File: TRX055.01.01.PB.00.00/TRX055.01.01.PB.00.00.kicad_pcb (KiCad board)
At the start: 4 copper layers, 91.3 x 139.8 mm, 164 parts, among them J1 DF40HC-80DS, J2 DF40HC-80DS, J3 DF40HC-80DS, J4 DF40HC-80DS, J5 SFP, J6 Micro_SD_Card, U1 XC7Z015-1CLG485I, U11 KSZ9031RNXCA, U12 USB3320C-EZK-TR, U14 W25Q128JVSIQ, U2 K4B4G1646E-BYMA, U3 K4B4G1646E-BYMA, U5 AP22913CN4, U9 AP22913CN4

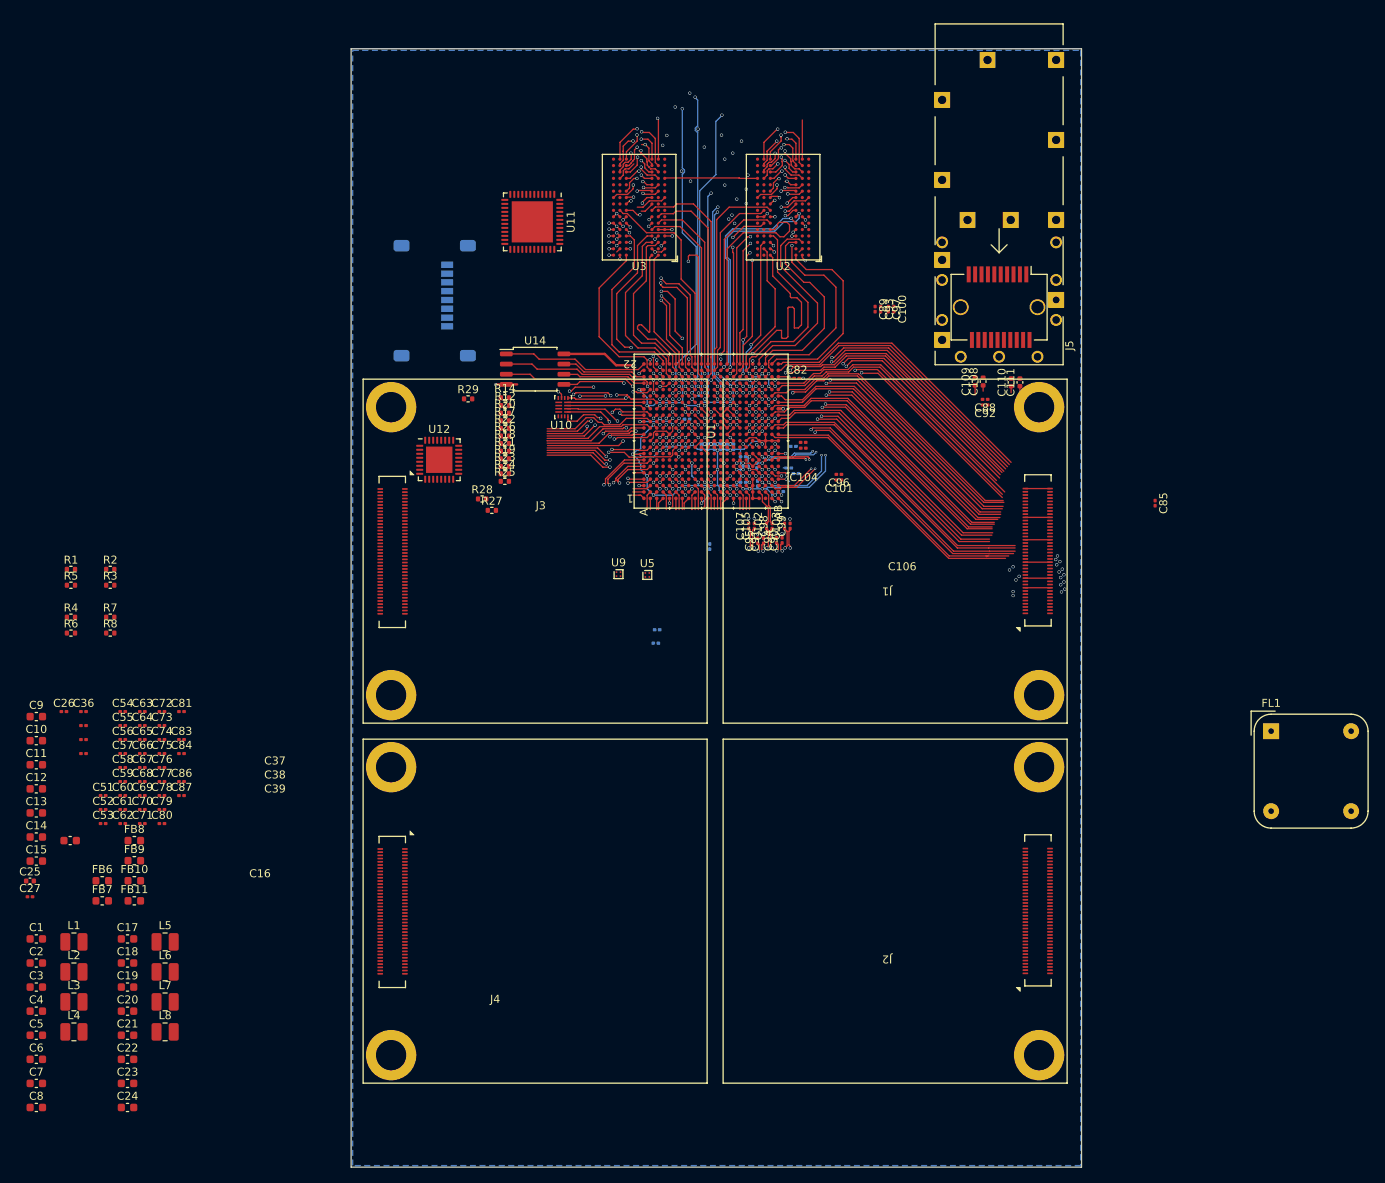
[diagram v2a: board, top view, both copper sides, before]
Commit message: +ETH +USB +Connectors
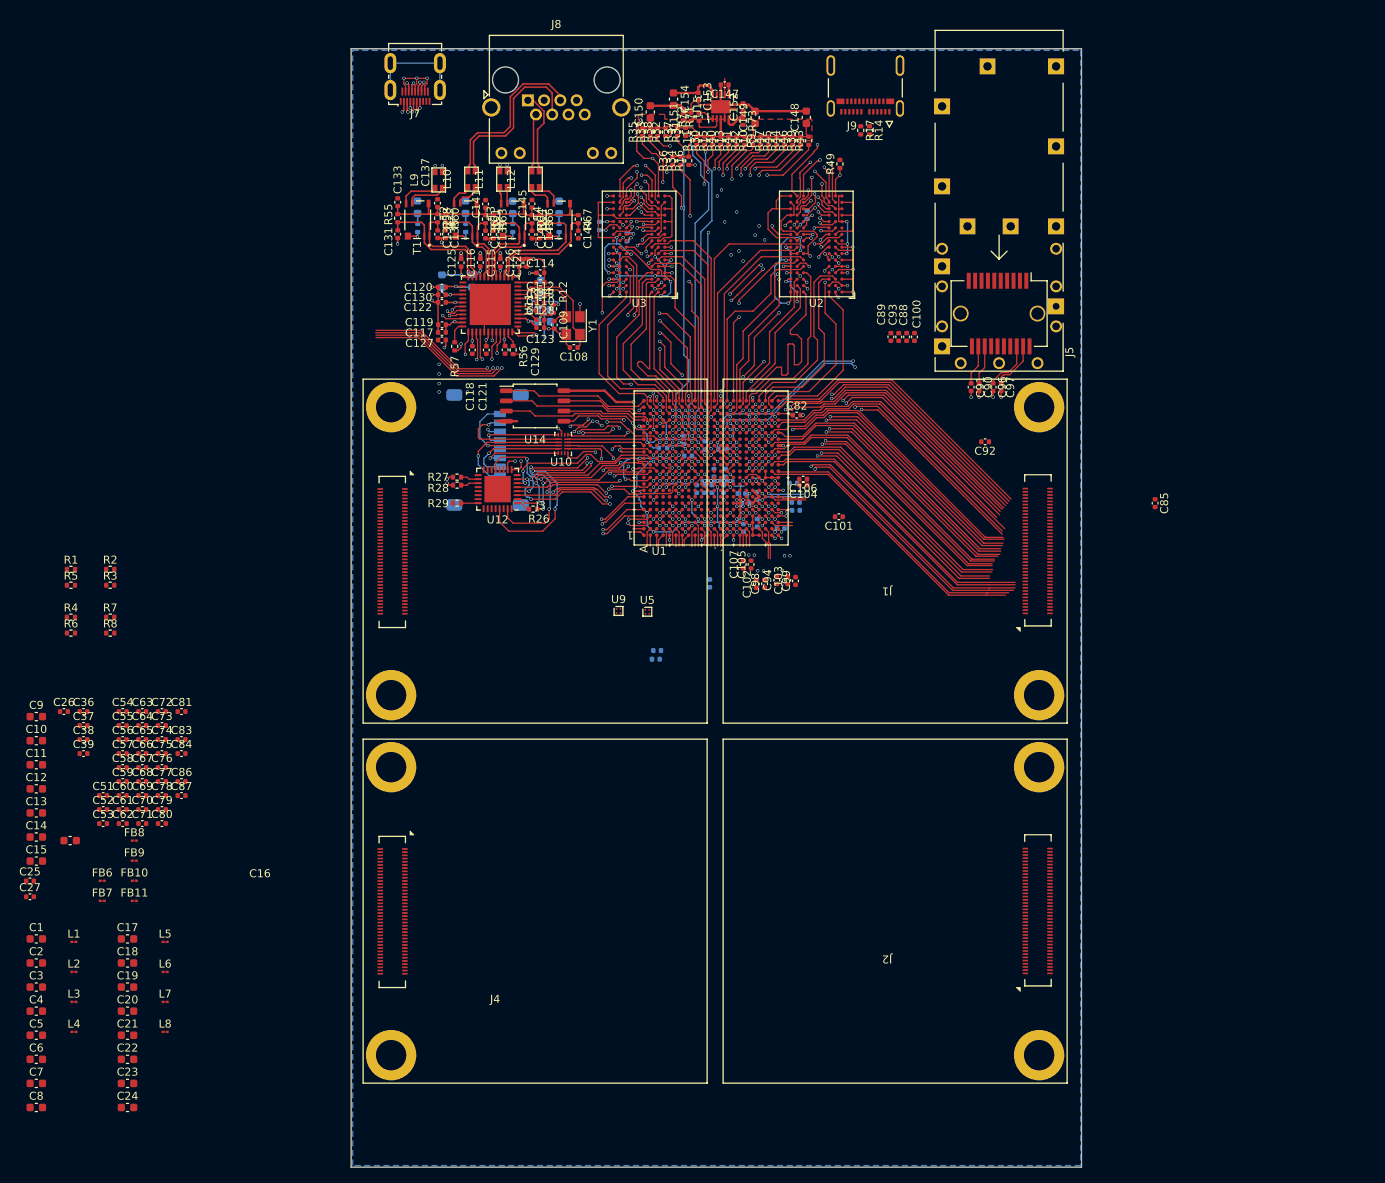
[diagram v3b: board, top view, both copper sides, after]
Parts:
- removed C111: M1, Capacitor_SMD:C_0402_1005Metric
- removed C95: M1, Capacitor_SMD:C_0201_0603Metric
- removed FL1: Choke_Schaffner_RN102-0.3-02-12M, Inductor_THT:Choke_Schaffner_RN102-04-14.0x14.0mm
- removed R18, R19, R20, R21, R22, R23, R24, R25: 33R, Resistor_SMD:R_0402_1005Metric
- added C112: M1, Capacitor_SMD:C_0402_1005Metric, F.Cu at (83.7, 61.0)
- added C113: 1M, Capacitor_SMD:C_0402_1005Metric, F.Cu at (83.7, 62.0)
- added C114: 1M, Capacitor_SMD:C_0402_1005Metric, F.Cu at (83.7, 58.2)
- added C115: M1, Capacitor_SMD:C_0402_1005Metric, F.Cu at (78.7, 57.0)
- added C116: M1, Capacitor_SMD:C_0402_1005Metric, F.Cu at (76.2, 56.9)
- added C117: 1M, Capacitor_SMD:C_0402_1005Metric, F.Cu at (71.3, 65.7)
- added C118: M1, Capacitor_SMD:C_0402_1005Metric, F.Cu at (75.2, 67.8)
- added C119: M1, Capacitor_SMD:C_0402_1005Metric, F.Cu at (71.4, 64.7)
- added C120: M1, Capacitor_SMD:C_0402_1005Metric, F.Cu at (71.3, 60.0)
- added C121: M1, Capacitor_SMD:C_0402_1005Metric, F.Cu at (76.9, 67.8)
- added C122: M1, Capacitor_SMD:C_0402_1005Metric, F.Cu at (71.3, 61.9)
- added C123: M1, Capacitor_SMD:C_0402_1005Metric, F.Cu at (83.7, 65.0)
- added C124: 1M, Capacitor_SMD:C_0402_1005Metric, F.Cu at (82.0, 57.0)
- added C125: M1, Capacitor_SMD:C_0402_1005Metric, F.Cu at (73.8, 57.0)
- added C126: M1, Capacitor_SMD:C_0402_1005Metric, F.Cu at (81.0, 57.0)
- added C127: 1M, Capacitor_SMD:C_0402_1005Metric, F.Cu at (71.3, 66.6)
- added C128: M1, Capacitor_SMD:C_0402_1005Metric, F.Cu at (83.7, 64.1)
- added C129: M1, Capacitor_SMD:C_0402_1005Metric, F.Cu at (79.2, 67.8)
- added C130: M1, Capacitor_SMD:C_0402_1005Metric, F.Cu at (71.3, 61.0)
- added C131: 10P, Capacitor_SMD:C_0402_1005Metric, F.Cu at (65.8, 53.4)
- added C132: 10P, Capacitor_SMD:C_0402_1005Metric, F.Cu at (70.8, 53.4)
- added C133: M1, Capacitor_SMD:C_0402_1005Metric, F.Cu at (65.8, 49.4)
- added C134: 1N, Capacitor_SMD:C_0603_1608Metric, B.Cu at (68.3, 50.0)
- added C135: 10P, Capacitor_SMD:C_0402_1005Metric, F.Cu at (71.8, 53.4)
- added C136: 10P, Capacitor_SMD:C_0402_1005Metric, F.Cu at (76.8, 53.4)
- added C137: M1, Capacitor_SMD:C_0402_1005Metric, F.Cu at (70.8, 49.5)
- added C138: 1N, Capacitor_SMD:C_0603_1608Metric, B.Cu at (74.3, 50.0)
- added C139: 10P, Capacitor_SMD:C_0402_1005Metric, F.Cu at (77.8, 53.4)
- added C140: 10P, Capacitor_SMD:C_0402_1005Metric, F.Cu at (82.6, 53.4)
- added C141: M1, Capacitor_SMD:C_0402_1005Metric, F.Cu at (76.8, 49.6)
- added C142: 1N, Capacitor_SMD:C_0603_1608Metric, B.Cu at (80.2, 50.0)
- added C143: 10P, Capacitor_SMD:C_0402_1005Metric, F.Cu at (83.6, 53.4)
- added C144: 10P, Capacitor_SMD:C_0402_1005Metric, F.Cu at (88.4, 53.4)
- added C145: M1, Capacitor_SMD:C_0402_1005Metric, F.Cu at (82.6, 49.6)
- added C146: 1N, Capacitor_SMD:C_0603_1608Metric, B.Cu at (86.0, 50.0)
- added C147: M1, Capacitor_SMD:C_0402_1005Metric, F.Cu at (106.7, 34.7)
- added C148: 10M, Capacitor_SMD:C_0603_1608Metric, F.Cu at (116.9, 38.8)
- added C149: 10M, Capacitor_SMD:C_0603_1608Metric, F.Cu at (110.5, 38.8)
- added C150: 10M, Capacitor_SMD:C_0603_1608Metric, F.Cu at (97.4, 38.1)
- added C151: M1, Capacitor_SMD:C_0402_1005Metric, F.Cu at (101.5, 38.7)
- added C152: M1, Capacitor_SMD:C_0402_1005Metric, F.Cu at (109.0, 37.5)
- added C153: M1, Capacitor_SMD:C_0402_1005Metric, F.Cu at (103.4, 36.2)
- added C154: 10M, Capacitor_SMD:C_0603_1608Metric, F.Cu at (100.3, 36.5)
- added FB1: GZ1608D601TF, Inductor_SMD:L_0603_1608Metric, B.Cu at (75.1, 59.2)
- added FB2: GZ1608D601TF, Inductor_SMD:L_0603_1608Metric, B.Cu at (84.1, 64.3)
- added FB3: GZ1608D601TF, Inductor_SMD:L_0603_1608Metric, B.Cu at (71.3, 59.2)
- added FB4: GZ1608D601TF, Inductor_SMD:L_0603_1608Metric, B.Cu at (84.1, 62.8)
- added FB5: GZ1608D601TF, Inductor_SMD:L_0603_1608Metric, B.Cu at (83.7, 59.9)
- added J7: HDMI_D_1.4, foot-ppa-passive:HDMI_Micro-D_Molex_46765-1x01, F.Cu at (68.0, 32.0)
- added J8: RJHSE5383, Connector_RJ:RJ45_Amphenol_RJHSE538X, F.Cu at (82.1, 36.6)
- added J9: 1054500101, 1054500101:MOLEX_1054500101, F.Cu at (124.3, 30.5)
- added L10: SRF2012A-801Y, foot-ppa-passive:SRF2012A-801Y, F.Cu at (75.0, 46.5)
- added L11: SRF2012A-801Y, foot-ppa-passive:SRF2012A-801Y, F.Cu at (79.0, 46.5)
- added L12: SRF2012A-801Y, foot-ppa-passive:SRF2012A-801Y, F.Cu at (83.0, 46.5)
- added L9: SRF2012A-801Y, foot-ppa-passive:SRF2012A-801Y, F.Cu at (70.9, 46.6)
- added R10: 39R, Resistor_SMD:R_0402_1005Metric, F.Cu at (110.2, 41.7)
- added R11: 39R, Resistor_SMD:R_0402_1005Metric, F.Cu at (103.2, 41.7)
- added R13: 39R, Resistor_SMD:R_0402_1005Metric, F.Cu at (107.2, 41.7)
- added R15: 39R, Resistor_SMD:R_0402_1005Metric, F.Cu at (105.2, 41.7)
- added R16: 39R, Resistor_SMD:R_0402_1005Metric, F.Cu at (102.2, 44.2)
- added R30: 39R, Resistor_SMD:R_0402_1005Metric, F.Cu at (104.2, 41.7)
- added R31: 39R, Resistor_SMD:R_0402_1005Metric, F.Cu at (101.8, 40.6)
- added R32: 39R, Resistor_SMD:R_0402_1005Metric, F.Cu at (99.3, 40.6)
- added R33: 39R, Resistor_SMD:R_0402_1005Metric, F.Cu at (97.4, 40.6)
- added R34: 39R, Resistor_SMD:R_0402_1005Metric, F.Cu at (101.2, 44.2)
- added R35: 39R, Resistor_SMD:R_0402_1005Metric, F.Cu at (96.4, 40.6)
- added R36: 39R, Resistor_SMD:R_0402_1005Metric, F.Cu at (100.2, 44.2)
- added R37: 39R, Resistor_SMD:R_0402_1005Metric, F.Cu at (100.8, 40.6)
- added R38: 39R, Resistor_SMD:R_0402_1005Metric, F.Cu at (98.3, 40.6)
- added R39: 39R, Resistor_SMD:R_0402_1005Metric, F.Cu at (116.2, 41.7)
- added R40: 39R, Resistor_SMD:R_0402_1005Metric, F.Cu at (106.2, 41.7)
- added R41: 39R, Resistor_SMD:R_0402_1005Metric, F.Cu at (108.2, 41.7)
- added R42: 39R, Resistor_SMD:R_0402_1005Metric, F.Cu at (109.2, 41.7)
- added R43: 39R, Resistor_SMD:R_0402_1005Metric, F.Cu at (117.2, 41.7)
- added R44: 39R, Resistor_SMD:R_0402_1005Metric, F.Cu at (114.2, 41.7)
- added R45: 39R, Resistor_SMD:R_0402_1005Metric, F.Cu at (113.2, 41.7)
- added R46: 39R, Resistor_SMD:R_0402_1005Metric, F.Cu at (115.2, 41.7)
- added R47: 39R, Resistor_SMD:R_0402_1005Metric, F.Cu at (112.2, 41.7)
- added R48: 80R, Resistor_SMD:R_0402_1005Metric, B.Cu at (94.5, 53.8)
- added R49: 10K, Resistor_SMD:R_0402_1005Metric, F.Cu at (121.1, 44.6)
- added R50: 240R, Resistor_SMD:R_0402_1005Metric, B.Cu at (117.0, 51.0)
- added R51: 240R, Resistor_SMD:R_0402_1005Metric, B.Cu at (91.0, 52.4)
- added R52: 80R, Resistor_SMD:R_0402_1005Metric, B.Cu at (106.4, 80.2)
- added R53: 80R, Resistor_SMD:R_0402_1005Metric, B.Cu at (104.2, 79.8)
- added R54: ???, Resistor_SMD:R_0402_1005Metric, F.Cu at (83.7, 59.5)
- added R55: 49R9, Resistor_SMD:R_0402_1005Metric, F.Cu at (65.8, 51.4)
- added R56: 33R, Resistor_SMD:R_0402_1005Metric, F.Cu at (80.2, 67.8)
- added R57: 33R, Resistor_SMD:R_0402_1005Metric, F.Cu at (73.0, 67.4)
- added R58: 49R9, Resistor_SMD:R_0402_1005Metric, F.Cu at (70.8, 51.4)
- added R59: 75R, Resistor_SMD:R_0402_1005Metric, B.Cu at (68.3, 52.6)
- added R60: 49R9, Resistor_SMD:R_0402_1005Metric, F.Cu at (71.8, 51.4)
- added R61: 49R9, Resistor_SMD:R_0402_1005Metric, F.Cu at (76.8, 51.5)
- added R62: 75R, Resistor_SMD:R_0402_1005Metric, B.Cu at (74.3, 52.6)
- added R63: 49R9, Resistor_SMD:R_0402_1005Metric, F.Cu at (77.8, 51.5)
- added R64: 49R9, Resistor_SMD:R_0402_1005Metric, F.Cu at (82.6, 51.5)
- added R65: 75R, Resistor_SMD:R_0402_1005Metric, B.Cu at (80.2, 52.6)
- added R66: 49R9, Resistor_SMD:R_0402_1005Metric, F.Cu at (83.6, 51.5)
- added R67: 49R9, Resistor_SMD:R_0402_1005Metric, F.Cu at (88.4, 51.5)
- added R68: 75R, Resistor_SMD:R_0402_1005Metric, B.Cu at (86.0, 52.6)
- added R69: 10K, Resistor_SMD:R_0402_1005Metric, B.Cu at (101.6, 79.1)
- added R70: 10K, Resistor_SMD:R_0402_1005Metric, B.Cu at (99.0, 80.1)
- added R71: 10K, Resistor_SMD:R_0402_1005Metric, F.Cu at (103.5, 38.7)
- added R72: 10K, Resistor_SMD:R_0402_1005Metric, F.Cu at (102.5, 38.7)
- added R73: 33R, Resistor_SMD:R_0402_1005Metric, F.Cu at (109.0, 39.2)
- added R9: 39R, Resistor_SMD:R_0402_1005Metric, F.Cu at (111.2, 41.7)
- added T1: SM453229-231N7Y, snapeda:XFMR_SM453229-231N7Y, F.Cu at (68.3, 51.6)
- added T2: SM453229-231N7Y, snapeda:XFMR_SM453229-231N7Y, F.Cu at (74.3, 51.6)
- added T3: SM453229-231N7Y, snapeda:XFMR_SM453229-231N7Y, F.Cu at (80.2, 51.6)
- added T4: SM453229-231N7Y, snapeda:XFMR_SM453229-231N7Y, F.Cu at (86.0, 51.6)
- added U15: TPS51200DRC, Package_SON:VSON-10-1EP_3x3mm_P0.5mm_EP1.65x2.4mm, F.Cu at (106.2, 37.5)
- added Y1: X322525MOB4SI, Crystal:Crystal_SMD_3225-4Pin_3.2x2.5mm, F.Cu at (87.8, 64.8)
- C100, C101, C102, C103, C104, C105, C106, C107, C26, C27, C28, C29, C30, C31, C32, C33, C34, C35, C36, C37, C38, C39, C40, C41, C42, C43, C44, C45, C46, C47, C48, C49, C50, C51, C52, C53, C54, C55, C56, C57, C58, C59, C60, C61, C62, C63, C64, C65, C66, C67, C68, C69, C70, C71, C72, C73, C74, C75, C76, C77, C78, C79, C80, C81, C82, C83, C84, C85, C86, C87, C88, C89, C90, C91, C92, C93, C94, C96, C97, C98, C99: footprint Capacitor_SMD:C_0201_0603Metric -> Capacitor_SMD:C_0402_1005Metric
- C108, C109: value M1 -> 10P
- FB10, FB11, FB6, FB7, FB8, FB9: footprint Inductor_SMD:L_0603_1608Metric -> Resistor_SMD:R_01005_0402Metric
- L1, L2, L3, L4, L5, L6, L7, L8: footprint Inductor_SMD:L_1008_2520Metric -> Resistor_SMD:R_01005_0402Metric
- R12: value 33R -> 10K
- moved C110 59.5 mm to (83.7, 63.0), turned to 0 degrees
- moved R17 57.4 mm to (123.7, 40.4), turned to -90 degrees
- moved R14 56.5 mm to (124.8, 40.4), turned to -90 degrees
- moved C109 53.1 mm to (85.4, 64.7), turned to -90 degrees
- moved C108 51.3 mm to (87.8, 67.5), turned to 180 degrees
- moved C91 32.3 mm to (137.5, 72.5), turned to -90 degrees
- moved C90 31.2 mm to (138.5, 72.5), turned to -90 degrees
- moved C96 22.1 mm to (140.2, 72.5), turned to -90 degrees
- moved J6 19.8 mm to (76.5, 80.3)
- moved C97 17.1 mm to (141.2, 72.5)
- moved R12 13.5 mm to (85.3, 62.7), turned to -90 degrees
- moved R29 13.1 mm to (73.2, 87.0)
- moved C88 12.5 mm to (129.4, 66.2), turned to -90 degrees
- moved U11 11.6 mm to (77.4, 62.2)
- moved R26 9.81 mm to (82.8, 87.8)
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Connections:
- C108 pad 1: Net-(J5-RD+) -> Net-(U11-XI)
- C108 pad 2: /SFP_Port/SFP_RX_P -> GND
- C109 pad 1: Net-(J5-RD-) -> Net-(U11-XO)
- C109 pad 2: /SFP_Port/SFP_RX_N -> GND
- C110 pad 1: Net-(J5-TD+) -> Net-(U11-RESET_N)
- C110 pad 2: /SFP_Port/SFP_TX_P -> GND
- C12 pad 1: /ZynqPower/1V8_RAIL_A -> +1V8
- C36 pad 1: VCC_MIO -> +1V8
- C37 pad 1: VCC_MIO -> +1V8
- C38 pad 1: VCC_MIO -> +1V8
- C39 pad 1: VCC_MIO -> +1V8
- C57 pad 1: /ZynqPower/1V8_RAIL_A -> +1V8
- C58 pad 1: /ZynqPower/1V8_RAIL_A -> +1V8
- C59 pad 1: /ZynqPower/1V8_RAIL_A -> +1V8
- C60 pad 1: /ZynqPower/1V8_RAIL_A -> +1V8
- C61 pad 1: /ZynqPower/VCCDDR -> VDD_DDR
- C62 pad 1: /ZynqPower/VCCDDR -> VDD_DDR
- C63 pad 1: /ZynqPower/VCCDDR -> VDD_DDR
- C64 pad 1: /ZynqPower/VCCDDR -> VDD_DDR
- C65 pad 1: /ZynqPower/VCCDDR -> VDD_DDR
- C66 pad 1: /ZynqPower/VCCDDR -> VDD_DDR
- C67 pad 1: /ZynqPower/VCCDDR -> VDD_DDR
- C68 pad 1: /ZynqPower/VCCDDR -> VDD_DDR
- C69 pad 1: /ZynqPower/VCCDDR -> VDD_DDR
- C7 pad 1: /ZynqPower/1V8_RAIL_A -> +1V8
- C8 pad 1: /ZynqPower/1V8_RAIL_A -> +1V8
- FB11 pad 1: VCC_MIO -> +1V8
- FB6 pad 1: /ZynqPower/1V8_RAIL_A -> +1V8
- FB7 pad 2: /ZynqPower/VCCDDR -> VDD_DDR
- J5 pad 12: Net-(J5-RD-) -> /GT_RX0_N
- J5 pad 13: Net-(J5-RD+) -> /GT_RX0_P
- J5 pad 15: Net-(J5-VccR) -> +3V3
- J5 pad 16: Net-(J5-VccR) -> +3V3
- J5 pad 18: Net-(J5-TD+) -> /GT_TX0_P
- J5 pad 19: Net-(J5-TD-) -> /GT_TX0_N
- J6 pad 1: unconnected-(J6-DAT2-Pad1) -> Net-(J6-DAT2)
- J6 pad 2: unconnected-(J6-DAT3/CD-Pad2) -> Net-(J6-DAT3/CD)
- J6 pad 3: unconnected-(J6-CMD-Pad3) -> Net-(J6-CMD)
- J6 pad 4: unconnected-(J6-VDD-Pad4) -> +3V3
- J6 pad 5: unconnected-(J6-CLK-Pad5) -> Net-(J6-CLK)
- J6 pad 6: unconnected-(J6-VSS-Pad6) -> GND
- J6 pad 7: unconnected-(J6-DAT0-Pad7) -> Net-(J6-DAT0)
- J6 pad 8: unconnected-(J6-DAT1-Pad8) -> Net-(J6-DAT1)
- J6 pad 9: unconnected-(J6-SHIELD-Pad9) -> GND
- L4 pad 2: /ZynqPower/1V8_RAIL_A -> +1V8
- R12 pad 1: Net-(U12-NXT) -> DVDDH
- R12 pad 2: /Zynq_PSMIO/MIO_ULPI_NXT -> Net-(U11-RESET_N)
- R14 pad 1: Net-(U12-STP) -> /USB_C/USBC_DP
- R14 pad 2: /Zynq_PSMIO/MIO_ULPI_STP -> /USB_C/USB_DP
- R17 pad 1: Net-(U12-DIR) -> /USB_C/USBC_DM
- R17 pad 2: /Zynq_PSMIO/MIO_ULPI_DIR -> /USB_C/USB_DM
- R27 pad 1: unconnected-(R27-Pad1) -> /USB_C/USB_DP
- R28 pad 1: unconnected-(R28-Pad1) -> /USB_C/USB_DM
- U1 pad A13: VCC_MIO -> +1V8
- U1 pad A4: unconnected-(U1B-IO_L10N_T1_AD11N_35-PadA4) -> /TMDS_D0_P
- U1 pad A5: unconnected-(U1B-IO_L10P_T1_AD11P_35-PadA5) -> /TMDS_D0_N
- U1 pad A6: unconnected-(U1B-IO_L9N_T1_DQS_AD3N_35-PadA6) -> /TMDS_CLK_P
- U1 pad A7: unconnected-(U1B-IO_L9P_T1_DQS_AD3P_35-PadA7) -> /TMDS_CLK_N
- U1 pad B10: VCC_MIO -> +1V8
- U1 pad B20: VCC_MIO -> +1V8
- U1 pad B3: unconnected-(U1B-IO_L13N_T2_MRCC_35-PadB3) -> /TMDS_D2_P
- U1 pad B4: unconnected-(U1B-IO_L13P_T2_MRCC_35-PadB4) -> /TMDS_D2_N
- U1 pad C11: unconnected-(U1D-PS_MIO53_501-PadC11) -> /ETH_PHY_Metal/SMI_MDIO
- U1 pad C17: VCC_MIO -> +1V8
- U1 pad D13: unconnected-(U1D-PS_MIO52_501-PadD13) -> /ETH_PHY_Metal/SMI_MDC
- U1 pad D14: VCC_MIO -> +1V8
- U1 pad E11: VCC_MIO -> +1V8
- U1 pad E21: /ZynqPower/VCCDDR -> VDD_DDR
- U1 pad E5: unconnected-(U1B-IO_L5N_T0_AD9N_35-PadE5) -> /TMDS_D1_P
- U1 pad F15: unconnected-(U1E-PS_MIO_VREF_501-PadF15) -> /ZynqPower/PS_MIO_VREF_501
- U1 pad F18: /ZynqPower/VCCDDR -> VDD_DDR
- U1 pad F5: unconnected-(U1B-IO_L5P_T0_AD9P_35-PadF5) -> /TMDS_D1_N
- U1 pad H16: unconnected-(U1E-PS_DDR_VREF0_502-PadH16) -> /ZynqPower/DDRVREF
- U1 pad H22: /ZynqPower/VCCDDR -> VDD_DDR
- U1 pad J19: /ZynqPower/VCCDDR -> VDD_DDR
- U1 pad K14: /ZynqPower/1V8_RAIL_A -> +1V8
- U1 pad K16: /ZynqPower/VCCDDR -> VDD_DDR
- U1 pad L13: /ZynqPower/1V8_RAIL_A -> +1V8
- U1 pad M14: /ZynqPower/1V8_RAIL_A -> +1V8
- U1 pad M16: unconnected-(U1C-PS_DDR_VRN_502-PadM16) -> Net-(U1C-PS_DDR_VRN_502)
- U1 pad M20: /ZynqPower/VCCDDR -> VDD_DDR
- U1 pad N13: VCC_MIO -> +1V8
- U1 pad N16: unconnected-(U1C-PS_DDR_VRP_502-PadN16) -> Net-(U1C-PS_DDR_VRP_502)
- U1 pad N17: /ZynqPower/VCCDDR -> VDD_DDR
- U1 pad P12: VCC_MIO -> +1V8
- U1 pad P14: /ZynqPower/1V8_RAIL_A -> +1V8
- U1 pad P16: unconnected-(U1E-PS_DDR_VREF1_502-PadP16) -> /ZynqPower/DDRVREF
- U1 pad R13: VCC_MIO -> +1V8
- U1 pad R21: /ZynqPower/VCCDDR -> VDD_DDR
- U1 pad T12: VCC_MIO -> +1V8
- U1 pad V22: /ZynqPower/VCCDDR -> VDD_DDR
- U10 pad 10: unconnected-(U10-DAT0B-Pad10) -> Net-(J6-DAT2)
- U10 pad 11: unconnected-(U10-DAT3B-Pad11) -> Net-(J6-DAT1)
- U10 pad 12: unconnected-(U10-DAT2B-Pad12) -> Net-(J6-DAT3/CD)
- U10 pad 13: unconnected-(U10-CMDB-Pad13) -> Net-(J6-CMD)
- U10 pad 15: VCC_MIO -> +1V8
- U10 pad 8: unconnected-(U10-CLKB-Pad8) -> Net-(J6-CLK)
- U10 pad 9: unconnected-(U10-DAT1B-Pad9) -> Net-(J6-DAT0)
- U11 pad 1: unconnected-(U11-AVDDH-Pad1) -> AVDDH
- U11 pad 10: unconnected-(U11-TXRXP_D-Pad10) -> /ETH_PHY_Metal/ETH_Pair/MDI_IN_P
- U11 pad 11: unconnected-(U11-TXRXM_D-Pad11) -> /ETH_PHY_Metal/ETH_Pair/MDI_IN_N
- U11 pad 12: unconnected-(U11-AVDDH-Pad12) -> AVDDH
- U11 pad 14: unconnected-(U11-DVDDL-Pad14) -> DVDDL
- U11 pad 16: unconnected-(U11-DVDDH-Pad16) -> DVDDH
- U11 pad 18: unconnected-(U11-DVDDL-Pad18) -> DVDDL
- U11 pad 19: unconnected-(U11-TXD0-Pad19) -> /Zynq_PSMIO/MIO_RGMII_TX0
- U11 pad 2: unconnected-(U11-TXRXP_A-Pad2) -> /ETH_PHY_Metal/ETH_Pair3/MDI_IN_P
- U11 pad 20: unconnected-(U11-TXD1-Pad20) -> /Zynq_PSMIO/MIO_RGMII_TX1
- U11 pad 21: unconnected-(U11-TXD2-Pad21) -> /Zynq_PSMIO/MIO_RGMII_TX2
- U11 pad 22: unconnected-(U11-TXD3-Pad22) -> /Zynq_PSMIO/MIO_RGMII_TX3
- U11 pad 23: unconnected-(U11-DVDDL-Pad23) -> DVDDL
- U11 pad 24: unconnected-(U11-GTX_CLK-Pad24) -> Net-(U11-GTX_CLK)
- U11 pad 25: unconnected-(U11-TX_EN-Pad25) -> /Zynq_PSMIO/MIO_RGMII_TX_CTL
- U11 pad 26: unconnected-(U11-DVDDL-Pad26) -> DVDDL
- U11 pad 27: unconnected-(U11-RXD3/MODE3-Pad27) -> /Zynq_PSMIO/MIO_RGMII_RX3
- U11 pad 28: unconnected-(U11-RXD2/MODE2-Pad28) -> /Zynq_PSMIO/MIO_RGMII_RX2
- U11 pad 29: unconnected-(U11-VSS-Pad29) -> GND
- U11 pad 3: unconnected-(U11-TXRXM_A-Pad3) -> /ETH_PHY_Metal/ETH_Pair3/MDI_IN_N
- U11 pad 30: unconnected-(U11-DVDDL-Pad30) -> DVDDL
- U11 pad 31: unconnected-(U11-RXD1/MODE1-Pad31) -> /Zynq_PSMIO/MIO_RGMII_RX1
- U11 pad 32: unconnected-(U11-RXD0/MODE0-Pad32) -> /Zynq_PSMIO/MIO_RGMII_RX0
- U11 pad 33: unconnected-(U11-RX_DV/CLK125_EN-Pad33) -> /Zynq_PSMIO/MIO_RGMII_RX_CTL
- U11 pad 34: unconnected-(U11-DVDDH-Pad34) -> DVDDH
- U11 pad 35: unconnected-(U11-RX_CLK/PHYAD2-Pad35) -> Net-(U11-RX_CLK/PHYAD2)
- U11 pad 36: unconnected-(U11-MDC-Pad36) -> /ETH_PHY_Metal/SMI_MDC
- U11 pad 37: unconnected-(U11-MDIO-Pad37) -> /ETH_PHY_Metal/SMI_MDIO
- U11 pad 39: unconnected-(U11-DVDDL-Pad39) -> DVDDL
- U11 pad 4: unconnected-(U11-AVDDL-Pad4) -> AVDDL
- U11 pad 40: unconnected-(U11-DVDDH-Pad40) -> DVDDH
- U11 pad 42: unconnected-(U11-RESET_N-Pad42) -> Net-(U11-RESET_N)
- U11 pad 44: unconnected-(U11-AVDDL_PLL-Pad44) -> AVDDL_PLL
- U11 pad 45: unconnected-(U11-XO-Pad45) -> Net-(U11-XO)
- U11 pad 46: unconnected-(U11-XI-Pad46) -> Net-(U11-XI)
- U11 pad 48: unconnected-(U11-ISET-Pad48) -> Net-(U11-ISET)
- U11 pad 49: unconnected-(U11-PAD_GND-Pad49) -> GND
- U11 pad 5: unconnected-(U11-TXRXP_B-Pad5) -> /ETH_PHY_Metal/ETH_Pair2/MDI_IN_P
- U11 pad 6: unconnected-(U11-TXRXM_B-Pad6) -> /ETH_PHY_Metal/ETH_Pair2/MDI_IN_N
- U11 pad 7: unconnected-(U11-TXRXP_C-Pad7) -> /ETH_PHY_Metal/ETH_Pair1/MDI_IN_P
- U11 pad 8: unconnected-(U11-TXRXM_C-Pad8) -> /ETH_PHY_Metal/ETH_Pair1/MDI_IN_N
- U11 pad 9: unconnected-(U11-AVDDL-Pad9) -> AVDDL
- U12 pad 10: Net-(U12-DATA6) -> /Zynq_PSMIO/MIO_ULPI_D6
- U12 pad 13: Net-(U12-DATA7) -> /Zynq_PSMIO/MIO_ULPI_D7
- U12 pad 2: Net-(U12-NXT) -> /Zynq_PSMIO/MIO_ULPI_NXT
- U12 pad 20: unconnected-(U12-VDD33-Pad20) -> +3V3
- U12 pad 28: unconnected-(U12-VDD18-Pad28) -> +1V8
- U12 pad 29: Net-(U12-STP) -> /Zynq_PSMIO/MIO_ULPI_STP
- U12 pad 3: Net-(U12-DATA0) -> /Zynq_PSMIO/MIO_ULPI_D0
- U12 pad 30: unconnected-(U12-VDD18-Pad30) -> +1V8
- U12 pad 31: Net-(U12-DIR) -> /Zynq_PSMIO/MIO_ULPI_DIR
- U12 pad 32: VCC_MIO -> +1V8
- U12 pad 4: Net-(U12-DATA1) -> /Zynq_PSMIO/MIO_ULPI_D1
- U12 pad 5: Net-(U12-DATA2) -> /Zynq_PSMIO/MIO_ULPI_D2
- U12 pad 6: Net-(U12-DATA3) -> /Zynq_PSMIO/MIO_ULPI_D3
- U12 pad 7: Net-(U12-DATA4) -> /Zynq_PSMIO/MIO_ULPI_D4
- U12 pad 9: Net-(U12-DATA5) -> /Zynq_PSMIO/MIO_ULPI_D5
- U14 pad 8: VCC_MIO -> +1V8
- U2 pad A1: Net-(U2-VDDQ-PadA1) -> VDD_DDR
- U2 pad A8: Net-(U2-VDDQ-PadA1) -> VDD_DDR
- U2 pad C1: Net-(U2-VDDQ-PadA1) -> VDD_DDR
- U2 pad C9: Net-(U2-VDDQ-PadA1) -> VDD_DDR
- U2 pad D2: Net-(U2-VDDQ-PadA1) -> VDD_DDR
- U2 pad E9: Net-(U2-VDDQ-PadA1) -> VDD_DDR
- U2 pad F1: Net-(U2-VDDQ-PadA1) -> VDD_DDR
- U2 pad H1: unconnected-(U2-VREFDQ-PadH1) -> VREF_DDR
- U2 pad H2: Net-(U2-VDDQ-PadA1) -> VDD_DDR
- U2 pad H9: Net-(U2-VDDQ-PadA1) -> VDD_DDR
- U2 pad L8: unconnected-(U2-ZQ-PadL8) -> Net-(U2-ZQ)
- U2 pad M8: unconnected-(U2-VREFCA-PadM8) -> VREF_DDR
- U3 pad A1: Net-(U3-VDDQ-PadA1) -> VDD_DDR
- U3 pad A8: Net-(U3-VDDQ-PadA1) -> VDD_DDR
- U3 pad C1: Net-(U3-VDDQ-PadA1) -> VDD_DDR
- U3 pad C9: Net-(U3-VDDQ-PadA1) -> VDD_DDR
- U3 pad D2: Net-(U3-VDDQ-PadA1) -> VDD_DDR
- U3 pad E9: Net-(U3-VDDQ-PadA1) -> VDD_DDR
- U3 pad F1: Net-(U3-VDDQ-PadA1) -> VDD_DDR
- U3 pad H1: unconnected-(U3-VREFDQ-PadH1) -> VREF_DDR
- U3 pad H2: Net-(U3-VDDQ-PadA1) -> VDD_DDR
- U3 pad H9: Net-(U3-VDDQ-PadA1) -> VDD_DDR
- U3 pad L8: unconnected-(U3-ZQ-PadL8) -> Net-(U3-ZQ)
- U3 pad M8: unconnected-(U3-VREFCA-PadM8) -> VREF_DDR
- U5 pad A1: VCC_MIO -> +1V8
- U5 pad A2: /ZynqPower/1V8_RAIL_A -> +1V8
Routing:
- net VDD_DDR: track 14.1 -> 146.5 mm, vias 3 -> 31
- net /USB_C/USB_DP: track 0.00 -> 124.3 mm, vias 0 -> 1
- net /USB_C/USB_DM: track 0.00 -> 118.9 mm, vias 0 -> 1
- net /TMDS_D1_N: track 0.00 -> 95.9 mm, vias 0 -> 2
- net /TMDS_D1_P: track 0.00 -> 95.8 mm, vias 0 -> 2
- net GND: track 203.1 -> 293.9 mm, vias 75 -> 114
- net /TMDS_CLK_P: track 0.00 -> 86.6 mm, vias 0 -> 2
- net /TMDS_CLK_N: track 0.00 -> 86.1 mm, vias 0 -> 2
- net /TMDS_D2_P: track 0.00 -> 86.0 mm, vias 0 -> 2
- net /TMDS_D2_N: track 0.00 -> 85.5 mm, vias 0 -> 2
- net /TMDS_D0_P: track 0.00 -> 83.7 mm, vias 0 -> 2
- net /TMDS_D0_N: track 0.00 -> 83.3 mm, vias 0 -> 2
- net +1V8: track 0.00 -> 80.8 mm, vias 0 -> 14
- net VCC_MIO: track 54.9 -> 0.00 mm, vias 10 -> 0
- net +3V3: track 0.00 -> 42.6 mm
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- added copper zone on In1.Cu, net +1V8
- added copper zone on F.Cu, net VDD_DDR
- added copper zone on In1.Cu, net VDD_DDR
- removed copper zone on In1.Cu, net /ZynqPower/1V8_RAIL_A
- removed copper zone on In1.Cu, net /ZynqPower/VCCDDR
- removed copper zone on In1.Cu, net VCC_MIO
